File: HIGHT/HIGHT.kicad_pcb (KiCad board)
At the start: 2 copper layers, 48 x 50 mm, 3 parts

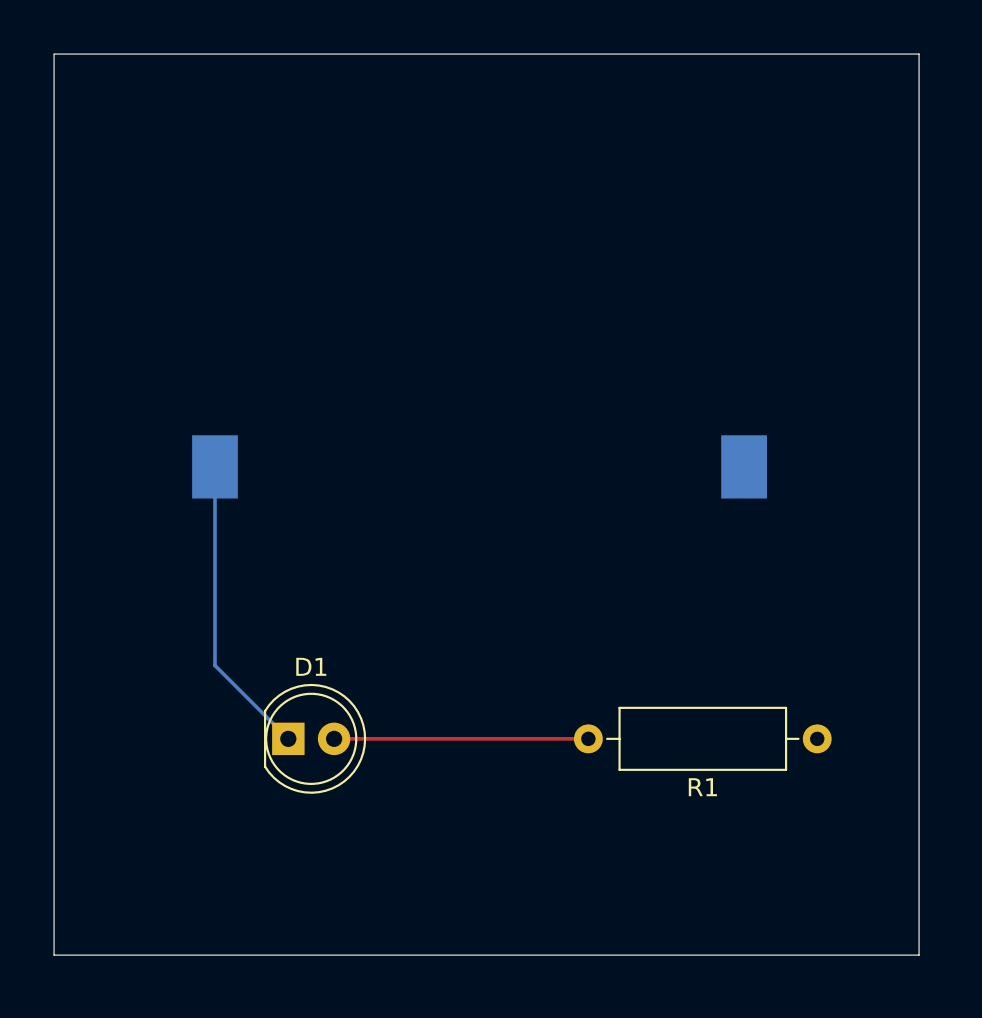
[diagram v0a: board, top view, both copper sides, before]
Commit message: Finished pcb design for Getting Started with KiCAD.
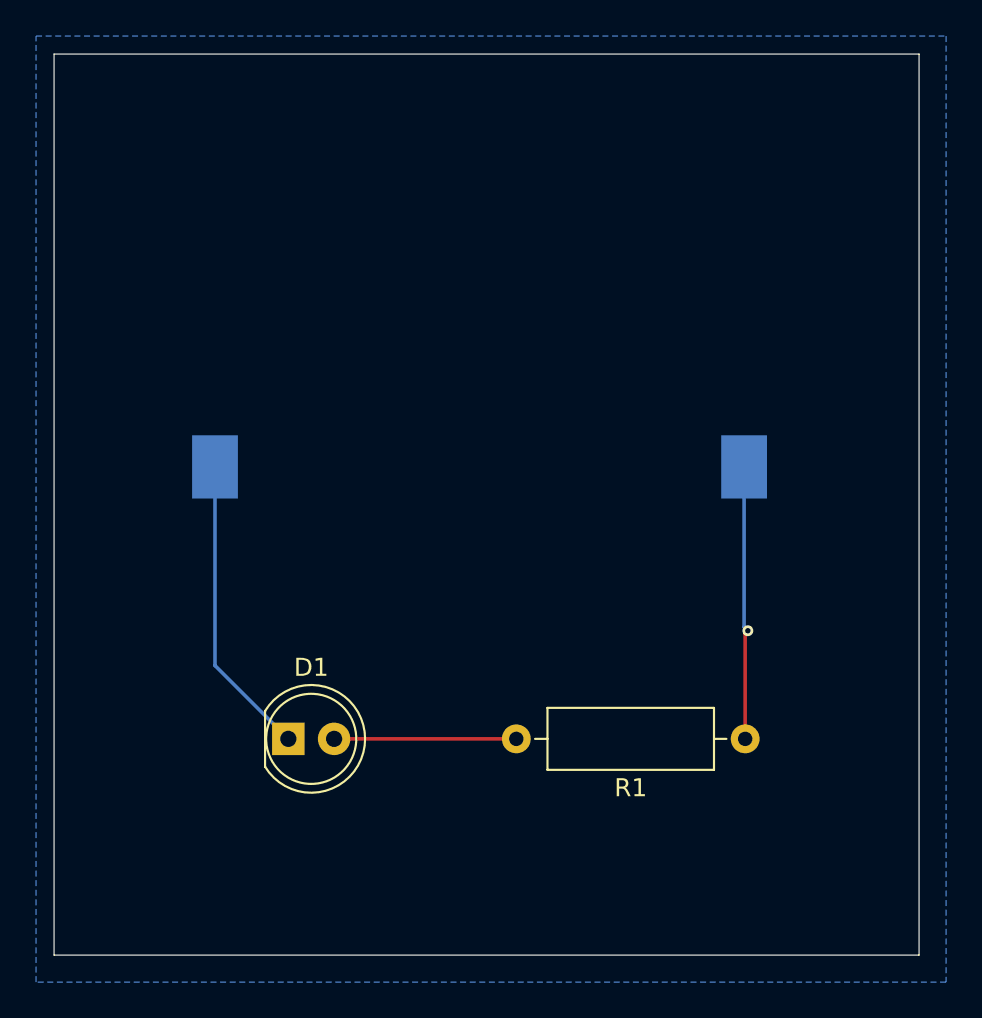
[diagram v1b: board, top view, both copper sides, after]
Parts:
- moved R1 4.00 mm to (87.3, 98.0)
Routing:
- net VCC: track 0.00 -> 15.2 mm, vias 0 -> 1
- net Net-(D1-A): track 14.1 -> 10.1 mm
- added copper zone on B.Cu, net GND
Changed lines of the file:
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@@
 			(outputformat 1)
 			(mirror no)
-			(drillshape 1)
+			(drillshape 0)
 			(scaleselection 1)
-			(outputdirectory "")
+			(outputdirectory "fabFiles/")
 		)
 	)
@@
 	(footprint "Resistor_THT:R_Axial_DIN0309_L9.0mm_D3.2mm_P12.70mm_Horizontal"
 		(layer "F.Cu")
-		(at 91.35 98 180)
+		(at 87.35 98 180)
 		(descr "Resistor, Axial_DIN0309 series, Axial, Horizontal, pin pitch=12.7mm, 0.5W = 1/2W, length*diameter=9*3.2mm^2, http://cdn-reichelt.de/documents/datenblatt/B400/1_4W%23YAG.pdf")
 		(tags "Resistor Axial_DIN0309 series Axial Horizontal pin pitch 12.7mm 0.5W = 1/2W length 9mm diameter 3.2mm")
@@
 	)
 	(segment
-		(start 78.65 98)
-		(end 64.54 98)
+		(start 87.35 92.15)
+		(end 87.35 98)
+		(width 0.2)
+		(layer "F.Cu")
+		(net 2)
+	)
+	(segment
+		(start 87.5 92)
+		(end 87.35 92.15)
+		(width 0.2)
+		(layer "F.Cu")
+		(net 2)
+	)
+	(via
+		(at 87.5 92)
+		(size 0.6)
+		(drill 0.3)
+		(layers "F.Cu" "B.Cu")
+		(net 2)
+	)
+	(segment
+		(start 87.29 82.90897)
+		(end 87.29 91.79)
+		(width 0.2)
+		(layer "B.Cu")
+		(net 2)
+	)
+	(segment
+		(start 87.29 91.79)
+		(end 87.5 92)
+		(width 0.2)
+		(layer "B.Cu")
+		(net 2)
+	)
+	(segment
+		(start 64.54 98)
+		(end 74.65 98)
 		(width 0.2)
 		(layer "F.Cu")
 		(net 3)
 	)
+	(zone
+		(net 1)
+		(net_name "GND")
+		(layer "B.Cu")
+		(hatch edge 0.5)
+		(connect_pads
+			(clearance 0.5)
+		)
+		(min_thickness 0.25)
+		(filled_areas_thickness no)
+		(fill yes
+			(thermal_gap 0.5)
+			(thermal_bridge_width 0.5)
+		)
+		(polygon
+			(pts
+				(xy 48 59) (xy 98.5 59) (xy 98.5 111.5) (xy 48 111.5)
+			)
+		)
+	)
 )
